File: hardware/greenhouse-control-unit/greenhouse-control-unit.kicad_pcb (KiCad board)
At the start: 2 copper layers, 150 x 90 mm, 51 parts, among them J1 Buck_Conn_01x01_Female, J10 Conn_01x08, J11 Conn_01x08, J12 Conn_01x05_Female, J15 Conn_01x05_Female, J16 Conn_01x05_Female, J2 Buck_Conn_01x01_Female, J3 Buck_Conn_01x01_Female, J4 Buck_Conn_01x01_Female, J5 Molex_KK-396_01x02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

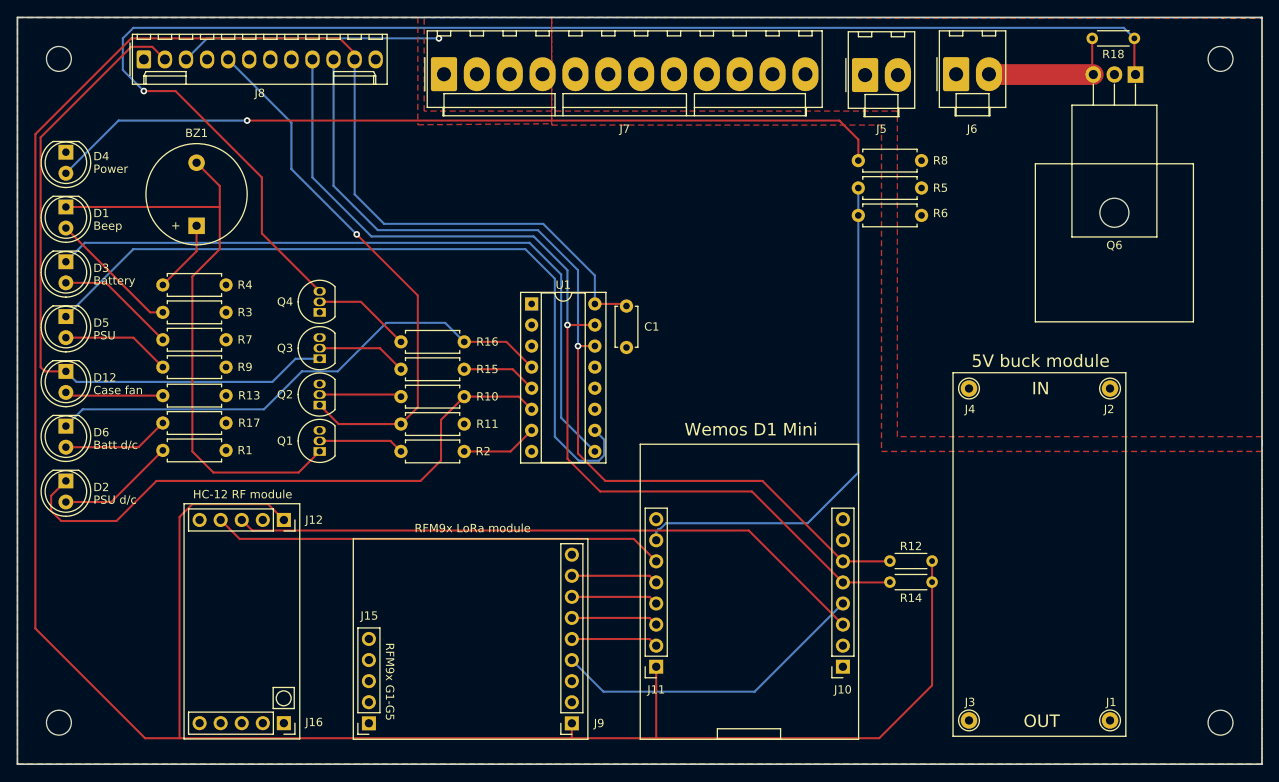
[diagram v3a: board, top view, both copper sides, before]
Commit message: Changed to 4 layer board
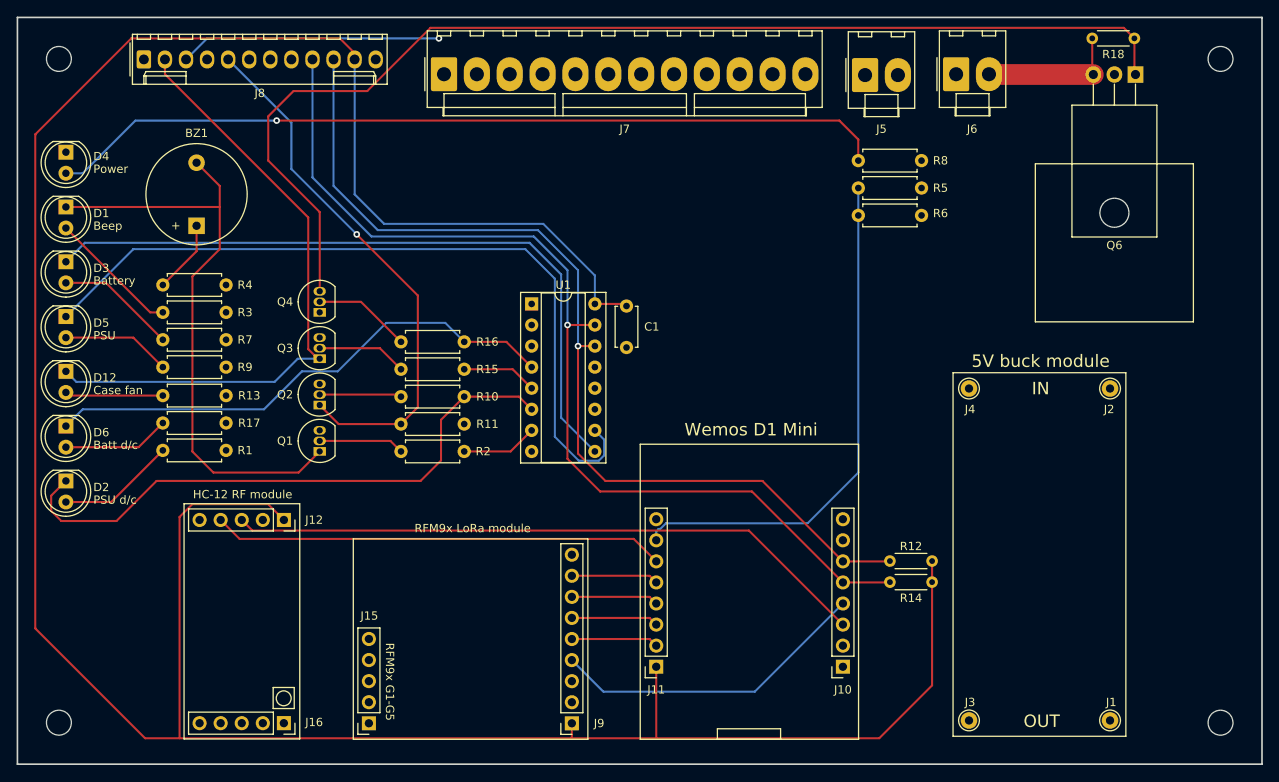
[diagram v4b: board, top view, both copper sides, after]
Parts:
- R4: value 1k -> 220R
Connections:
- net /HC12_RX renamed /D4
- net /I2C_SCL renamed /D1
- net /I2C_SDA renamed /D2
- net /RFM95_G0_IRQ renamed /D3
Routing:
- net Net-(Q4-Pad3): track 169.9 -> 137.4 mm, vias 1 -> 0
- net /CaseFan_Sink: track 83.4 -> 76.2 mm
- added copper zone on In1.Cu, net +10V
- added copper zone on In1.Cu, net +5V
- added copper zone on In2.Cu, net GND
- removed copper zone on F.Cu, net +10V
- removed copper zone on F.Cu, net +5V
- removed copper zone on B.Cu, net GND
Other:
- copper layers 2 -> 4

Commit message: Remove LEDs from PSU/batt d/c
Sharing IO pin causing gate/base to be pulled high and/or LED to be partially on
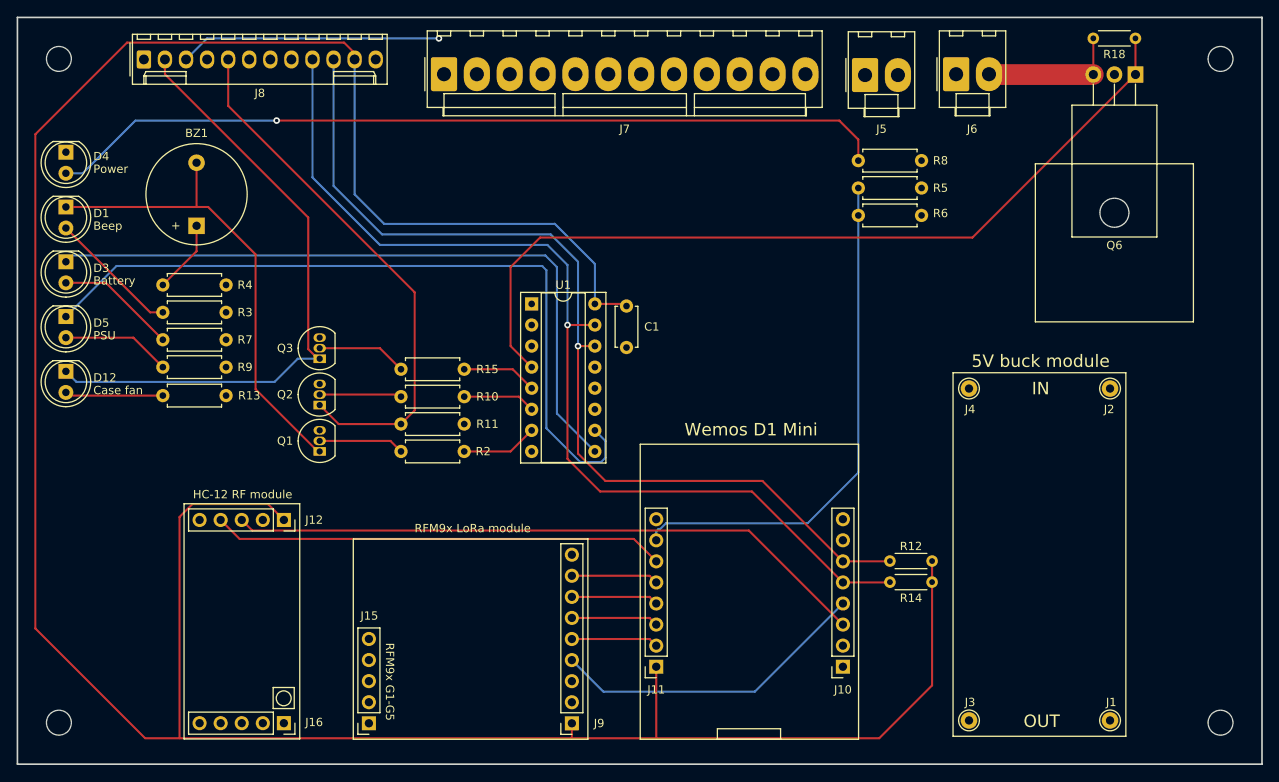
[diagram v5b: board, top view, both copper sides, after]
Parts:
- removed D2, D6: LED, LED_THT:LED_D5.0mm
- removed Q4: BC337, Package_TO_SOT_THT:TO-92_Inline
- removed R1, R17: 2k, Resistor_THT:R_Axial_DIN0207_L6.3mm_D2.5mm_P7.62mm_Horizontal
- removed R16: 10k, Resistor_THT:R_Axial_DIN0207_L6.3mm_D2.5mm_P7.62mm_Horizontal
- R11: value 10k -> 1k
- R15: value 10k -> 2k
- moved R18 0.13 mm to (206.9, 47.0)
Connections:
- net /D8 renamed /SCLK
- net /SR_BatteryLed renamed /IO_BatteryLed
- net /SR_Beep renamed /IO_Beep
- net /SR_CaseFan_EN renamed /IO_CaseFan_EN
- net /SR_PsuLed renamed /IO_PsuLed
- net /SR_PsuRelay_EN renamed /IO_PsuRelay_EN
- Q6 pad 1: Net-(Q4-Pad3) -> /IO_Batt_EN
- R18 pad 1: Net-(Q4-Pad3) -> /IO_Batt_EN
- U1 pad 4: /SR_Batt_EN -> /IO_Batt_EN
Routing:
- net Net-(Q4-Pad3): track 137.4 -> 0.00 mm
- net /IO_Batt_EN: track 0.00 -> 102.4 mm
- net /IO_PsuRelay_EN: track 72.5 -> 8.76 mm
- net /SR_Batt_EN: track 63.5 -> 0.00 mm
- net Net-(BZ1-Pad2): track 73.3 -> 57.6 mm
- net Net-(D2-Pad2): track 14.3 -> 0.00 mm
- net Net-(D6-Pad2): track 12.9 -> 0.00 mm
- net Net-(Q4-Pad2): track 11.8 -> 0.00 mm
- net /IO_PsuLed: track 93.7 -> 92.5 mm
- net /IO_BatteryLed: track 85.2 -> 84.2 mm
- net /D1: track 116.0 -> 116.6 mm
- net Net-(D12-Pad2): track 11.8 -> 11.3 mm
- net /PsuRelayNC_IN: track 65.0 -> 64.7 mm, vias 1 -> 0

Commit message: Add a bunch of BJTs
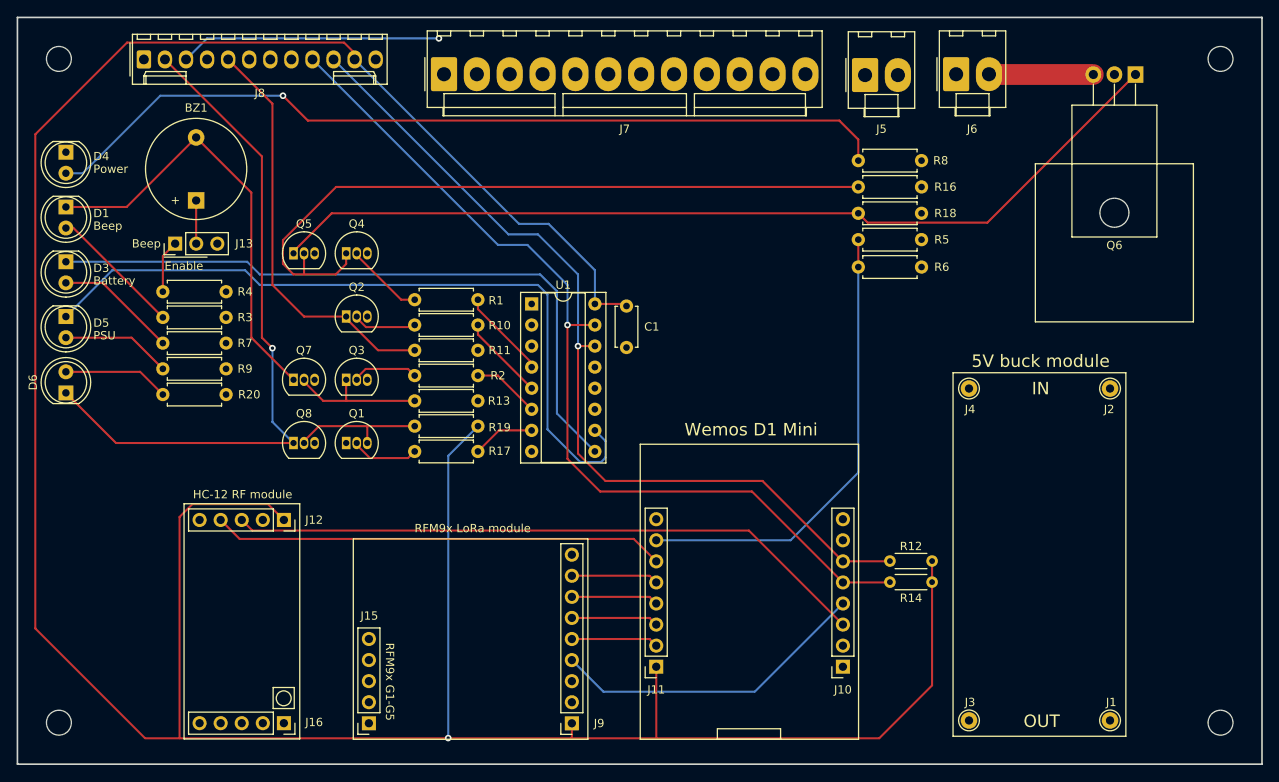
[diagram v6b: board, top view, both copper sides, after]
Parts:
- removed D12: LED, LED_THT:LED_D5.0mm
- removed R15: 2k, Resistor_THT:R_Axial_DIN0207_L6.3mm_D2.5mm_P7.62mm_Horizontal
- added D6: LED, LED_THT:LED_D5.0mm, F.Cu at (78.0, 89.7)
- added J13: Beep_Jumper, Connector_PinHeader_2.54mm:PinHeader_1x03_P2.54mm_Vertical, F.Cu at (91.1, 71.7)
- added Q4: BC337, Package_TO_SOT_THT:TO-92_Inline, F.Cu at (111.8, 72.9)
- added Q5: BC337, Package_TO_SOT_THT:TO-92_Inline, F.Cu at (105.4, 72.9)
- added Q7: BC337, Package_TO_SOT_THT:TO-92_Inline, F.Cu at (105.4, 88.1)
- added Q8: BC337, Package_TO_SOT_THT:TO-92_Inline, F.Cu at (105.4, 95.8)
- added R1: 100k, Resistor_THT:R_Axial_DIN0207_L6.3mm_D2.5mm_P7.62mm_Horizontal, F.Cu at (127.6, 78.5)
- added R16: 1k, Resistor_THT:R_Axial_DIN0207_L6.3mm_D2.5mm_P7.62mm_Horizontal, F.Cu at (181.1, 64.9)
- added R17: 2k, Resistor_THT:R_Axial_DIN0207_L6.3mm_D2.5mm_P7.62mm_Horizontal, F.Cu at (127.6, 96.8)
- added R19: 1k, Resistor_THT:R_Axial_DIN0207_L6.3mm_D2.5mm_P7.62mm_Horizontal, F.Cu at (127.6, 93.7)
- added R20: 2k, Resistor_THT:R_Axial_DIN0207_L6.3mm_D2.5mm_P7.62mm_Horizontal, F.Cu at (97.3, 89.9)
- BZ1: value Buzzer -> 10mA beep
- Q1: value BC337 -> BC557
- R13: value 2k -> 1k
- R18: footprint Resistor_THT:R_Axial_DIN0204_L3.6mm_D1.6mm_P5.08mm_Horizontal -> Resistor_THT:R_Axial_DIN0207_L6.3mm_D2.5mm_P7.62mm_Horizontal
- R2: value 10k -> 2k
- R4: value 220R -> 100R
- moved R18 33.3 mm to (181.1, 68.1)
- moved R13 30.4 mm to (127.6, 90.7)
- moved Q2 11.1 mm to (111.8, 80.5), turned to 0 degrees
- moved R2 9.29 mm to (127.6, 87.6)
- moved R11 9.04 mm to (127.6, 84.6)
- moved R10 8.79 mm to (127.6, 81.5)
- moved R6 6.22 mm to (173.5, 74.5)
- moved R5 6.22 mm to (181.1, 71.2)
- moved Q3 4.08 mm to (111.8, 88.1), turned to 0 degrees
- moved Q1 3.35 mm to (111.8, 95.8), turned to 0 degrees
- moved BZ1 3.05 mm to (93.7, 66.5)
- moved R4 0.81 mm to (97.3, 77.5)
- moved R3 0.61 mm to (97.3, 80.6)
- moved R7 0.41 mm to (97.3, 83.7)
- moved R9 0.20 mm to (97.3, 86.8)
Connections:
- net /SCLK renamed /D8
- Q1 pad 1: Net-(BZ1-Pad2) -> GND
- Q1 pad 2: Net-(Q1-Pad2) -> Net-(R17-Pad2)
- Q1 pad 3: GND -> Net-(Q8-Pad2)
- Q3 pad 1: /CaseFan_Sink -> Net-(Q3-Pad1)
- Q6 pad 1: /IO_Batt_EN -> Net-(Q5-Pad1)
- R13 pad 2: Net-(D12-Pad2) -> Net-(Q3-Pad1)
- R18 pad 1: /IO_Batt_EN -> +10V
- R18 pad 2: /Batt_GND -> Net-(Q5-Pad1)
- R2 pad 2: Net-(Q1-Pad2) -> Net-(Q3-Pad2)
- R4 pad 2: Net-(BZ1-Pad1) -> Net-(J13-Pad1)
- U1 pad 5: /IO_CaseFan_EN -> /IO_PsuRelay_EN
- U1 pad 6: /IO_PsuRelay_EN -> /IO_Beep
- U1 pad 7: /IO_Beep -> /IO_CaseFan_EN
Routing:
- net Net-(Q5-Pad1): track 0.00 -> 111.5 mm
- net /IO_Batt_EN: track 102.4 -> 10.8 mm
- net Net-(Q4-Pad1): track 0.00 -> 87.3 mm
- net +3V3: track 342.5 -> 371.6 mm, vias 0 -> 1
- net Net-(Q3-Pad1): track 0.00 -> 17.1 mm
- net Net-(Q8-Pad2): track 0.00 -> 16.3 mm
- net /PsuRelayNC_IN: track 64.7 -> 49.9 mm
- net Net-(D6-Pad2): track 0.00 -> 12.9 mm
- net Net-(D12-Pad2): track 11.3 -> 0.00 mm
- net Net-(Q1-Pad2): track 10.3 -> 0.00 mm
- net /D1: track 116.6 -> 106.8 mm
- net /D2: track 121.0 -> 111.2 mm
- net Net-(Q4-Pad2): track 0.00 -> 9.43 mm
- net Net-(R17-Pad2): track 0.00 -> 8.20 mm
- net /A0: track 62.7 -> 55.8 mm
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
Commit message: Overhauled transistors
PSU, battery, beep, fan
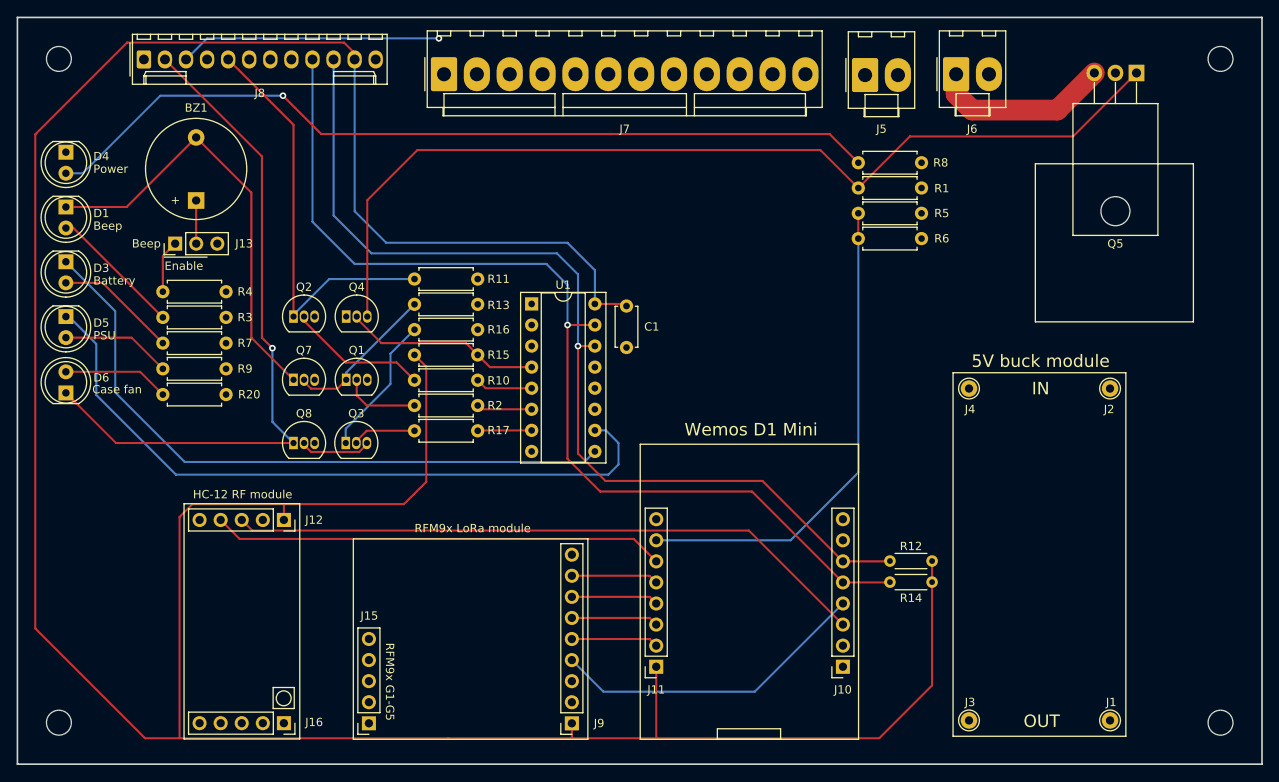
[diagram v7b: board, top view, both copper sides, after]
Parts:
- removed Q6: FDP7030BL, Package_TO_SOT_THT:TO-220-3_Horizontal_TabDown
- removed R18: 10k, Resistor_THT:R_Axial_DIN0207_L6.3mm_D2.5mm_P7.62mm_Horizontal
- removed R19: 1k, Resistor_THT:R_Axial_DIN0207_L6.3mm_D2.5mm_P7.62mm_Horizontal
- added R15: 10k, Resistor_THT:R_Axial_DIN0207_L6.3mm_D2.5mm_P7.62mm_Horizontal, F.Cu at (120.0, 85.1)
- Q1: value BC557 -> BC547
- Q2, Q3: value BC337 -> BC547
- Q4: value BC337 -> 2N7000
- Q5: value BC337 -> IRF4905; footprint Package_TO_SOT_THT:TO-92_Inline -> Package_TO_SOT_THT:TO-220-3_Horizontal_TabDown
- R1: value 100k -> 10k
- R10: value 100k -> 33k
- R17, R2: value 2k -> 33k
- moved Q5 103.9 mm to (207.0, 51.2), turned to 180 degrees
- moved R16 63.5 mm to (120.0, 82.1), turned to 0 degrees
- moved R1 55.1 mm to (181.1, 65.0)
- moved R13 11.6 mm to (127.6, 79.0)
- moved R11 8.59 mm to (127.6, 76.0)
- moved Q3 7.62 mm to (111.7, 95.8)
- moved Q4 7.62 mm to (111.8, 80.5)
- moved Q1 7.62 mm to (111.8, 88.1)
- moved R10 6.65 mm to (127.6, 88.2)
- moved Q2 6.35 mm to (105.4, 80.5)
- moved R2 3.61 mm to (127.6, 91.2)
- moved R6 3.43 mm to (173.5, 71.1)
- moved R5 3.17 mm to (181.1, 68.1)
- moved R17 2.49 mm to (127.6, 94.3)
- moved R8 0.25 mm to (181.1, 62.0)
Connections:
- J6 pad 1: +10V -> /Batt+10V
- J6 pad 2: /Batt_GND -> GND
- Q1 pad 1: GND -> Net-(Q7-Pad2)
- Q1 pad 2: Net-(R17-Pad2) -> Net-(R2-Pad2)
- Q1 pad 3: Net-(Q8-Pad2) -> GND
- Q3 pad 2: Net-(Q3-Pad2) -> Net-(R17-Pad2)
- Q3 pad 3: GND -> Net-(Q8-Pad2)
- Q4 pad 1: Net-(Q4-Pad1) -> GND
- Q4 pad 2: Net-(Q4-Pad2) -> /IO_Batt_EN
- Q4 pad 3: GND -> Net-(Q4-Pad3)
- Q5 pad 1: Net-(Q5-Pad1) -> Net-(Q4-Pad3)
- Q5 pad 2: Net-(Q4-Pad1) -> +10V
- Q5 pad 3: GND -> /Batt+10V
- Q7 pad 2: Net-(Q3-Pad1) -> Net-(Q7-Pad2)
- R1 pad 1: /IO_Batt_EN -> +10V
- R1 pad 2: Net-(Q4-Pad2) -> Net-(Q4-Pad3)
- R13 pad 2: Net-(Q3-Pad1) -> Net-(Q7-Pad2)
- R16 pad 1: +10V -> Net-(Q3-Pad1)
- R16 pad 2: Net-(Q4-Pad1) -> +5V
- R2 pad 2: Net-(Q3-Pad2) -> Net-(R2-Pad2)
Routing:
- net Net-(Q4-Pad3): track 0.00 -> 116.9 mm
- net Net-(Q5-Pad1): track 111.5 -> 0.00 mm
- net Net-(Q4-Pad1): track 87.3 -> 0.00 mm
- net /Batt+10V: track 0.00 -> 21.7 mm
- net Net-(Q7-Pad2): track 0.00 -> 18.4 mm
- net /IO_Batt_EN: track 10.8 -> 23.5 mm
- net /Batt_GND: track 12.5 -> 0.00 mm
- net /D2: track 111.2 -> 122.7 mm
- net /D1: track 106.8 -> 117.8 mm
- net Net-(Q4-Pad2): track 9.43 -> 0.00 mm
- net Net-(R2-Pad2): track 0.00 -> 9.34 mm
- net Net-(R10-Pad2): track 7.71 -> 16.3 mm
- net Net-(Q3-Pad2): track 7.99 -> 0.00 mm
- net Net-(Q8-Pad2): track 16.3 -> 8.68 mm
- net +3V3: track 371.6 -> 378.5 mm, vias 1 -> 0
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
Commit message: Swapped ESP8266 for ESP32
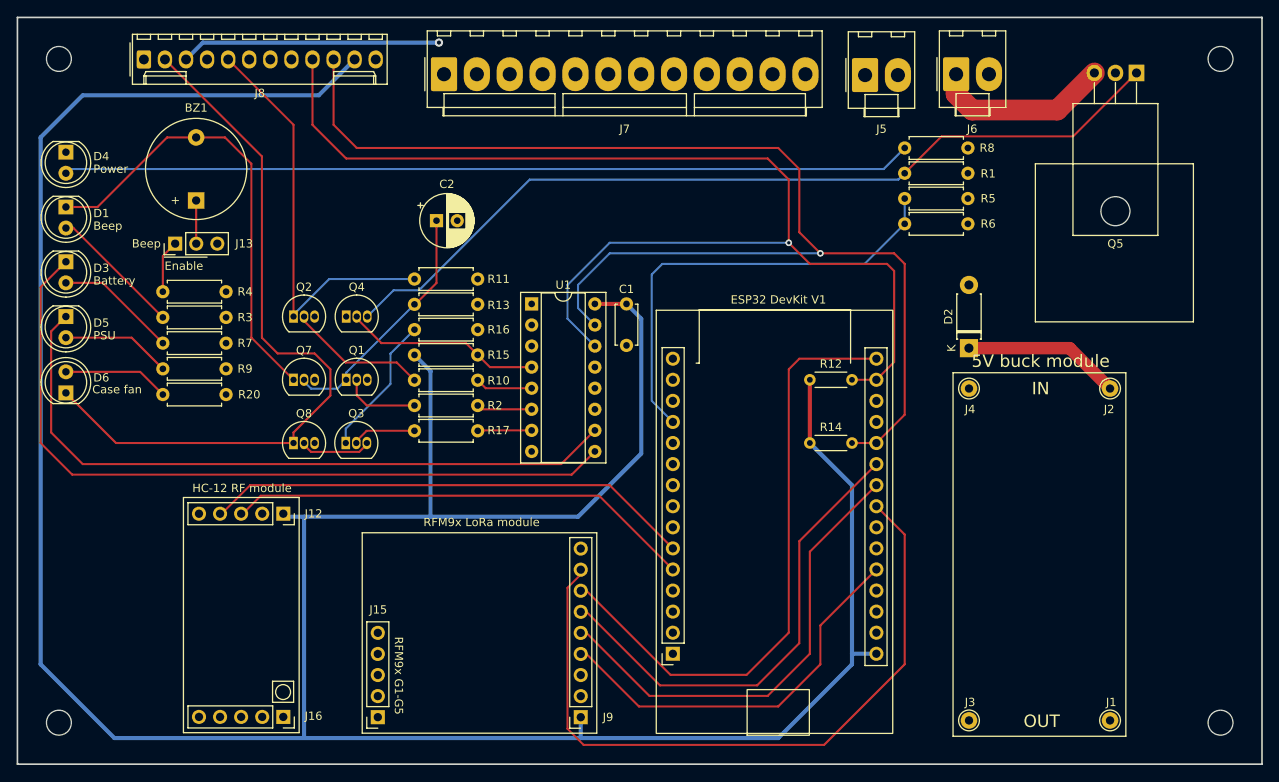
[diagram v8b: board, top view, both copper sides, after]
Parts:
- removed J11: Conn_01x08, Connector_PinSocket_2.54mm:PinSocket_1x08_P2.54mm_Vertical
- added C2: 100uF, Capacitor_THT:CP_Radial_D6.3mm_P2.50mm, F.Cu at (122.6, 69.0)
- added D2: D, Diode_THT:D_DO-41_SOD81_P7.62mm_Horizontal, F.Cu at (186.8, 84.3)
- J10: value Conn_01x08 -> Conn_ESP32_DevKitV1_Female; footprint Connector_PinSocket_2.54mm:PinSocket_1x08_P2.54mm_Vertical -> Nick:PinSocket_ESP32_DevKitV1
- moved R12 26.3 mm to (167.6, 88.1), turned to 0 degrees
- moved R14 22.3 mm to (167.6, 95.8), turned to 0 degrees
- moved J10 20.9 mm to (163.8, 103.4), turned to 0 degrees
- moved R5 5.86 mm to (186.7, 66.3)
- moved R6 5.86 mm to (179.1, 69.3)
- moved R1 5.86 mm to (186.7, 63.2)
- moved R8 5.86 mm to (186.7, 60.2)
- moved J15 1.30 mm to (115.6, 128.8)
- moved J9 1.30 mm to (140.0, 128.8)
- moved J12 0.76 mm to (104.2, 104.3)
- moved J16 0.76 mm to (104.2, 128.8)
- moved C1 0.25 mm to (145.5, 79.0)
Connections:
- J10 pad 2: GND -> unconnected-(J10-Pad2)
- J10 pad 3: /D4 -> unconnected-(J10-Pad3)
- J10 pad 4: /D3 -> unconnected-(J10-Pad4)
- J10 pad 5: /D2 -> /HC12_RX
- J10 pad 6: /D1 -> /HC12_TX
- J10 pad 7: /RX -> unconnected-(J10-Pad7)
- J10 pad 8: /TX -> unconnected-(J10-Pad8)
- J12 pad 3: /D4 -> /HC12_RX
- J12 pad 4: /D0 -> /HC12_TX
- J2 pad 1: +10V -> /Buck+10V
- J8 pad 10: /D1 -> /I2C_SDA
- J8 pad 9: /D2 -> /I2C_SCL
- J9 pad 4: /D3 -> /RFM95_IRQ
- J9 pad 5: /D8 -> /SCLK
- J9 pad 6: /D7 -> /MISO
- J9 pad 7: /D6 -> /MOSI
- J9 pad 8: /D5 -> /RFM95_CS
- R12 pad 2: /D1 -> /I2C_SCL
- R14 pad 2: /D2 -> /I2C_SDA
- R5 pad 2: /A0 -> /VSense
- R6 pad 1: /A0 -> /VSense
- U1 pad 14: /D1 -> /I2C_SCL
- U1 pad 15: /D2 -> /I2C_SDA
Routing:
- net /I2C_SDA: track 0.00 -> 150.5 mm, vias 0 -> 1
- net /I2C_SCL: track 0.00 -> 144.2 mm, vias 0 -> 1
- net /D2: track 122.7 -> 0.00 mm, vias 1 -> 0
- net /D1: track 117.8 -> 0.00 mm, vias 1 -> 0
- net /RFM95_CS: track 0.00 -> 86.1 mm
- net /D4: track 77.7 -> 0.00 mm
- net /MOSI: track 0.00 -> 73.6 mm
- net /HC12_TX: track 0.00 -> 59.0 mm
- net /A0: track 59.0 -> 0.00 mm
- net /MISO: track 0.00 -> 56.9 mm
- net /HC12_RX: track 0.00 -> 56.5 mm
- net /SCLK: track 0.00 -> 55.9 mm
- net /VSense: track 0.00 -> 54.9 mm
- net /D0: track 54.6 -> 0.00 mm
- net /RFM95_IRQ: track 0.00 -> 47.2 mm
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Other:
- board text removed: "Wemos D1 Mini"
